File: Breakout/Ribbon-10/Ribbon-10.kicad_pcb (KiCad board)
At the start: 2 copper layers, 24.1 x 36.8 mm, 5 parts, among them J1 Conn_02x05_Odd_Even, J2 Conn_01x10, J3 Conn_01x10

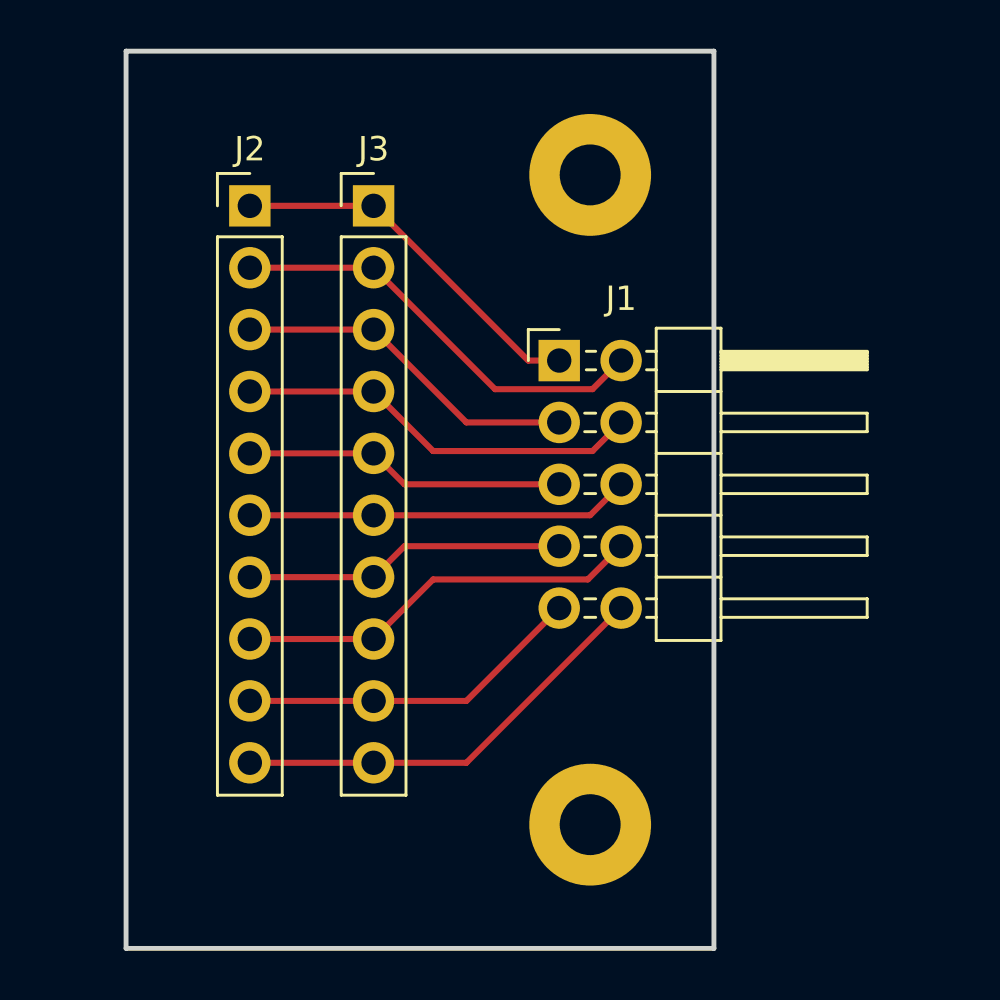
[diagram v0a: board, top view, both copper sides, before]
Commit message: Enlarge breakout board traces and add silkscreened title.
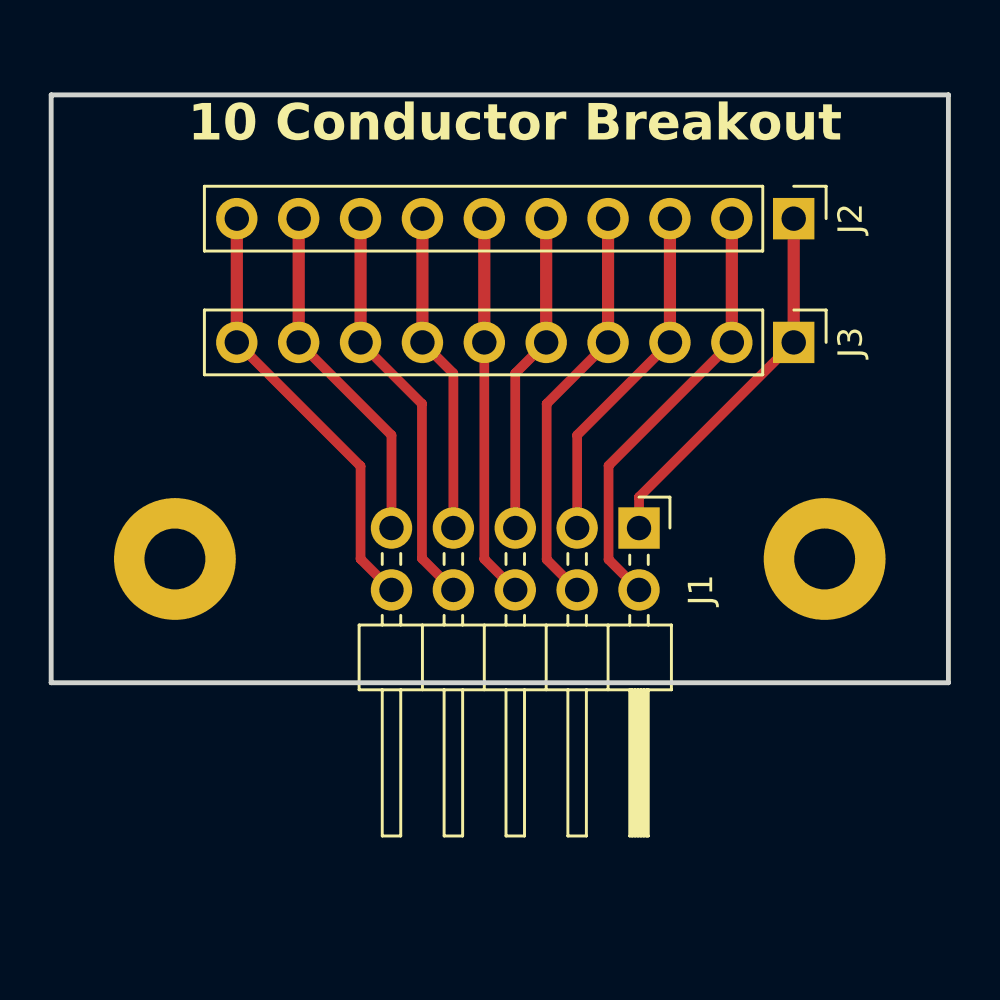
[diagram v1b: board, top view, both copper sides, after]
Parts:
- moved J2 22.3 mm to (169.6, 84.3), turned to -90 degrees
- moved REF2 20.2 mm to (144.2, 98.3), turned to -90 degrees
- moved REF1 18.5 mm to (170.9, 98.3), turned to -90 degrees
- moved J3 18.1 mm to (169.6, 89.4), turned to -90 degrees
- moved J1 7.62 mm to (163.3, 97.0), turned to -90 degrees
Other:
- board size 24.1 x 36.8 mm -> 36.8 x 24.1 mm
- board text added: "10 Conductor Breakout"
